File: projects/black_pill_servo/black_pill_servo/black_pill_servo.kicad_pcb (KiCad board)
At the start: 2 copper layers, 4 parts, among them J1 alim_logique_5V, U1 black_pill, U2 servo_connector, U3 w5500

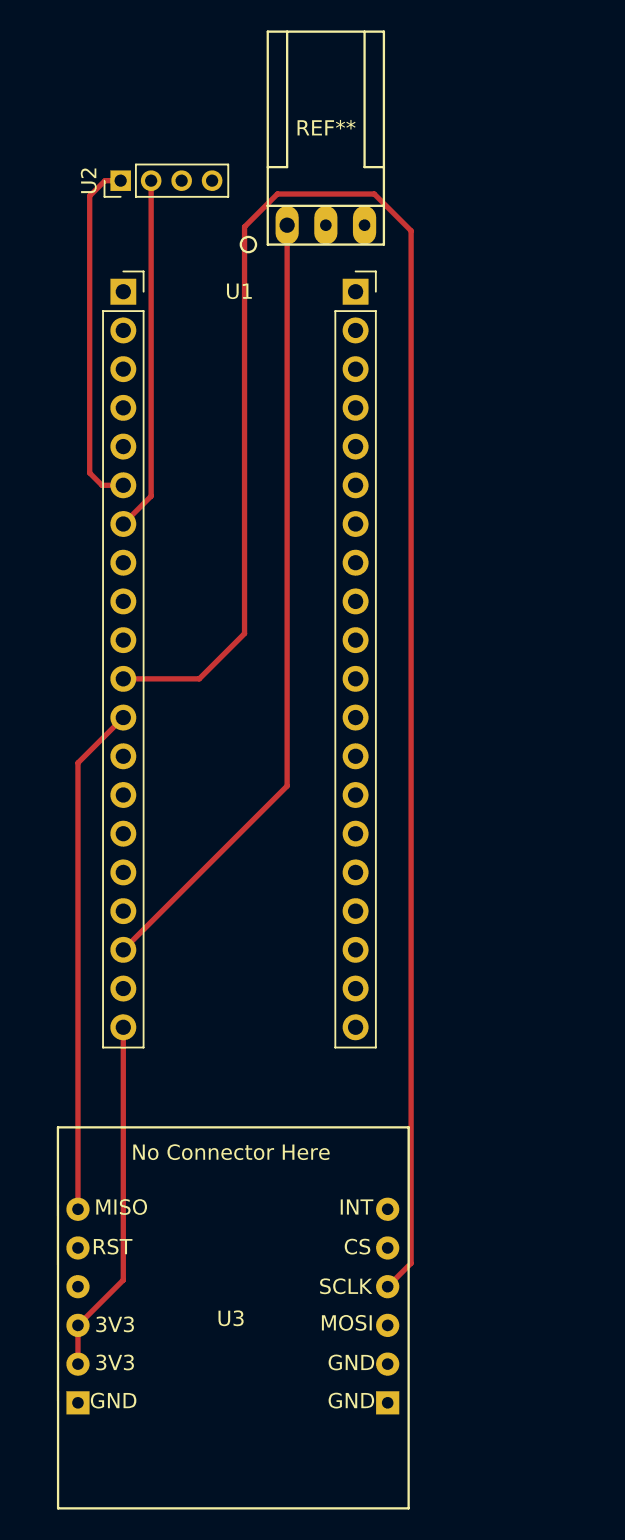
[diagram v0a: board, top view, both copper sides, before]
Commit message: Updated schematic & PCB for servo card.
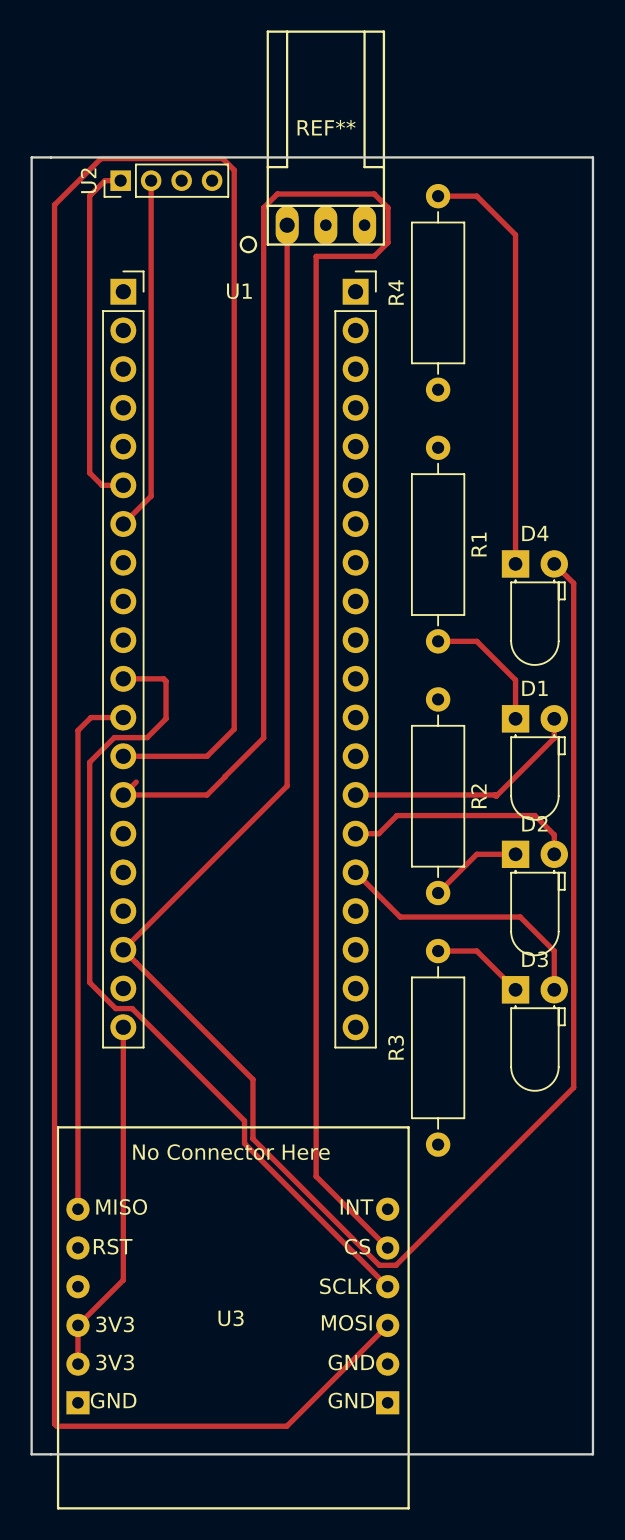
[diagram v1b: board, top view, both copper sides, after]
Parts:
- added D1: LED, LED_THT:LED_D3.0mm_Horizontal_O1.27mm_Z2.0mm_Clear, F.Cu at (188.0, 67.3)
- added D2: LED, LED_THT:LED_D3.0mm_Horizontal_O1.27mm_Z2.0mm_Clear, F.Cu at (188.0, 76.2)
- added D3: LED, LED_THT:LED_D3.0mm_Horizontal_O1.27mm_Z2.0mm_Clear, F.Cu at (188.0, 85.1)
- added D4: LED, LED_THT:LED_D3.0mm_Horizontal_O1.27mm_Z2.0mm_Clear, F.Cu at (188.0, 57.1)
- added R1: 180, Resistor_THT:R_Axial_DIN0309_L9.0mm_D3.2mm_P12.70mm_Horizontal, F.Cu at (182.9, 49.5)
- added R2: 180, Resistor_THT:R_Axial_DIN0309_L9.0mm_D3.2mm_P12.70mm_Horizontal, F.Cu at (182.9, 66.0)
- added R3: 180, Resistor_THT:R_Axial_DIN0309_L9.0mm_D3.2mm_P12.70mm_Horizontal, F.Cu at (182.9, 95.2)
- added R4: 180, Resistor_THT:R_Axial_DIN0309_L9.0mm_D3.2mm_P12.70mm_Horizontal, F.Cu at (182.9, 45.7)
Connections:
- U1 pad 14: Net-(U1-Pad14) -> CS
- U1 pad 34: Net-(U1-Pad34) -> COMMUNICATION_LED
- U1 pad 35: Net-(U1-Pad35) -> STARTED_LED
- U1 pad 36: Net-(U1-Pad36) -> HARDFAULT_LED
- U3 pad 2: Net-(U3-Pad2) -> CS
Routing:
- net MOSI: track 0.00 -> 162.8 mm
- net CS: track 0.00 -> 130.0 mm
- net +5V: track 52.0 -> 132.1 mm
- net SCLK: track 118.6 -> 54.7 mm
- net Net-(D4-Pad1): track 0.00 -> 27.7 mm
- net HARDFAULT_LED: track 0.00 -> 17.7 mm
- net COMMUNICATION_LED: track 0.00 -> 15.9 mm
- net STARTED_LED: track 0.00 -> 15.3 mm
- net Net-(D1-Pad1): track 0.00 -> 8.67 mm
- net Net-(D3-Pad1): track 0.00 -> 6.13 mm
- net Net-(D2-Pad1): track 0.00 -> 6.13 mm
- net MISO: track 33.5 -> 34.7 mm
- added copper zone on F.Cu, net GND
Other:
- board outline added: 36.8 x 85.1 mm
- net class Default: clearance 0.6 -> 0.2
- rule trace_clearance: 0.6 -> 0.2
